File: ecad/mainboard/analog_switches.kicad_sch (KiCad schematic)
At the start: 66 parts, among them U1 CD4051BM96, U10 DRV5056A3xQDBZxR, U11 DRV5056A3xQDBZxR, U12 DRV5056A3xQDBZxR, U13 DRV5056A3xQDBZxR, U14 DRV5056A3xQDBZxR, U15 DRV5056A3xQDBZxR, U16 DRV5056A3xQDBZxR, U17 DRV5056A3xQDBZxR, U18 DRV5056A3xQDBZxR, U19 DRV5056A3xQDBZxR, U20 DRV5056A3xQDBZxR, U23 DRV5056A3xQDBZxR, U5 DRV5056A3xQDBZxR, U6 DRV5056A3xQDBZxR, U7 DRV5056A3xQDBZxR, U8 DRV5056A3xQDBZxR, U9 CD4051BM96

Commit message: place parts except analog switches
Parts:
- U22: renamed from U1; JLCPCB (none) -> C21379
- U23: renamed from U9; JLCPCB (none) -> C21379
- U6: renamed from U23; JLCPCB (none) -> C2866615
- renumbered C19 to C21, C20 to C22, C22 to C23, C25 to C24, C23 to C25, C21 to C26, C24 to C27, C26 to C28, C27 to C29, C29 to C30, C33 to C32, C28 to C33, C30 to C34, C32 to C35, C34 to C36, C35 to C37, C39 to C38, C43 to C39, C47 to C40, C37 to C41, C41 to C42, C45 to C43, C49 to C44, C36 to C45, C40 to C46, C44 to C47, C38 to C49, C42 to C50, C46 to C51, C50 to C52, R11 to R14, R12 to R15, R13 to R16, R14 to R17, R15 to R18, R16 to R19, R17 to R20, R18 to R21, R19 to R22, R21 to R23, R23 to R24, R20 to R26, R22 to R27, R24 to R28, R28 to R29, U8 to U10, U10 to U11, U11 to U12, U12 to U13, U13 to U14, U17 to U16, U19 to U17, U14 to U18, U16 to U19, U18 to U20, U20 to U21, U5 to U7, U6 to U8, U7 to U9
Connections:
- net ADC0 renamed MUX0_OUT
- net ADC1 renamed MUX1_OUT
- net GPIO10 renamed MUX0_A
- net GPIO11 renamed MUX0_B
- net GPIO12 renamed MUX0_C
- net GPIO13 renamed MUX1_A
- net GPIO14 renamed MUX1_B
- net GPIO15 renamed MUX1_C

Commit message: .
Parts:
- U10, U11, U12, U13, U14, U15, U16, U17, U18, U19, U20, U21, U6, U7, U8, U9: footprint Package_TO_SOT_SMD:SOT-23 -> Udong:SW_Cherry_MX_PCB_1.00u_hall_effect
- renumbered C25 to C22, C22 to C23, C26 to C24, C23 to C25, C27 to C26, C24 to C27, C33 to C30, C30 to C31, C34 to C32, C31 to C33, C35 to C34, C32 to C35, C41 to C38, C38 to C39, C42 to C40, C39 to C41, C43 to C42, C40 to C43, C49 to C46, C46 to C47, C50 to C48, C47 to C49, C51 to C50, C48 to C51
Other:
- moved on the sheet: C22, C24, C26, C28, C30, C32, C34, C36, C38, C40, C42, C44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

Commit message: WIP: PCB case
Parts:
- U22, U23: JCSC (none) -> C21379; JLCPCB C21379 -> (none)
- U6: JCSC (none) -> C2866615; JLCPCB C2866615 -> (none)
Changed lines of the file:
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@@
 			)
 		)
-		(property "JLCPCB" "C2866615"
+		(property "JCSC" "C2866615"
 			(at 43.18 27.94 0)
 			(effects
@@
 			)
 		)
-		(property "JLCPCB" "C21379"
+		(property "JCSC" "C21379"
 			(at 118.11 168.91 0)
 			(effects
@@
 			)
 		)
-		(property "JLCPCB" "C21379"
+		(property "JCSC" "C21379"
 			(at 48.26 168.91 0)
 			(effects

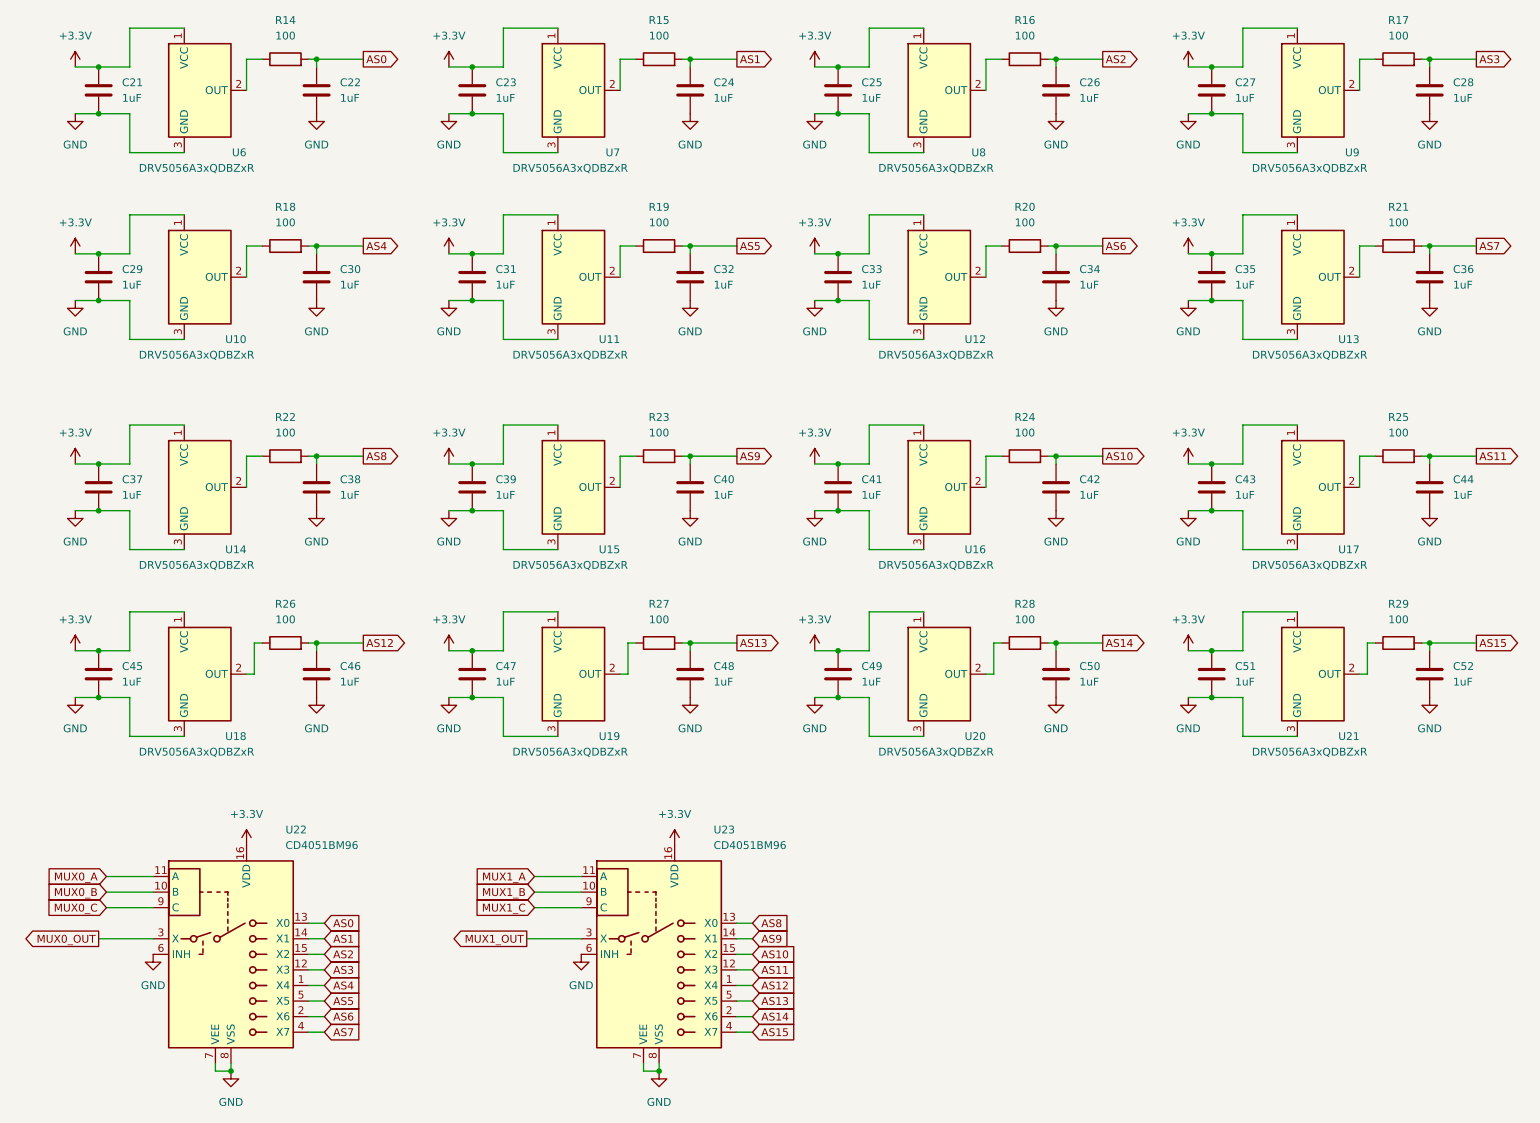
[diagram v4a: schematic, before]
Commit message: Make a DigitalSwitch field so that scripts can configure digital-switch related parts easily
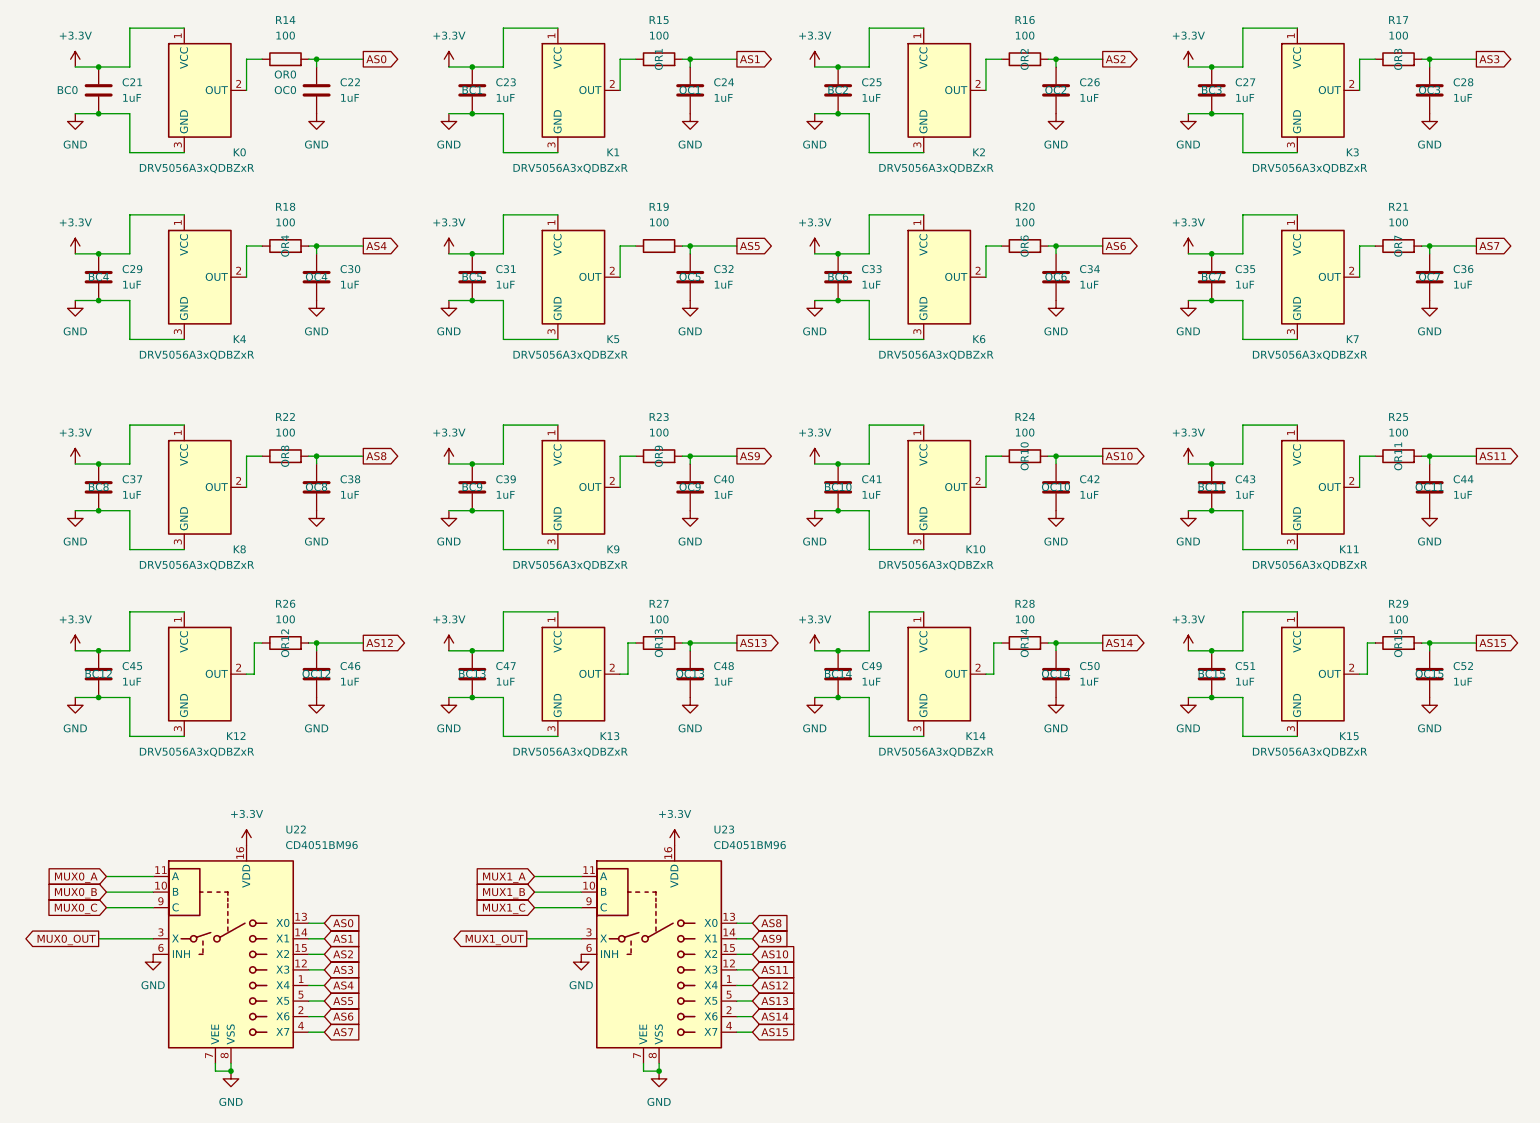
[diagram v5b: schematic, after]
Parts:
- C21: DigitalSwitch (none) -> BC0
- C22: DigitalSwitch (none) -> OC0
- C23: DigitalSwitch (none) -> BC1
- C24: DigitalSwitch (none) -> OC1
- C25: DigitalSwitch (none) -> BC2
- C26: DigitalSwitch (none) -> OC2
- C27: DigitalSwitch (none) -> BC3
- C28: DigitalSwitch (none) -> OC3
- C29: DigitalSwitch (none) -> BC4
- C30: DigitalSwitch (none) -> OC4
- C31: DigitalSwitch (none) -> BC5
- C32: DigitalSwitch (none) -> OC5
- C33: DigitalSwitch (none) -> BC6
- C34: DigitalSwitch (none) -> OC6
- C35: DigitalSwitch (none) -> BC7
- C36: DigitalSwitch (none) -> OC7
- C37: DigitalSwitch (none) -> BC8
- C38: DigitalSwitch (none) -> OC8
- C39: DigitalSwitch (none) -> BC9
- C40: DigitalSwitch (none) -> OC9
- C41: DigitalSwitch (none) -> BC10
- C42: DigitalSwitch (none) -> OC10
- C43: DigitalSwitch (none) -> BC11
- C44: DigitalSwitch (none) -> OC11
- C45: DigitalSwitch (none) -> BC12
- C46: DigitalSwitch (none) -> OC12
- C47: DigitalSwitch (none) -> BC13
- C48: DigitalSwitch (none) -> OC13
- C49: DigitalSwitch (none) -> BC14
- C50: DigitalSwitch (none) -> OC14
- C51: DigitalSwitch (none) -> BC15
- C52: DigitalSwitch (none) -> OC15
- K0: renamed from U6; footprint Udong:SW_Cherry_MX_PCB_1.00u_hall_effect -> Udong:SK20_hall_IC
- K1: renamed from U7; footprint Udong:SW_Cherry_MX_PCB_1.00u_hall_effect -> Udong:SK20_hall_IC
- K10: renamed from U16; footprint Udong:SW_Cherry_MX_PCB_1.00u_hall_effect -> Udong:SK20_hall_IC
- K11: renamed from U17; footprint Udong:SW_Cherry_MX_PCB_1.00u_hall_effect -> Udong:SK20_hall_IC
- K12: renamed from U18; footprint Udong:SW_Cherry_MX_PCB_1.00u_hall_effect -> Udong:SK20_hall_IC
- K13: renamed from U19; footprint Udong:SW_Cherry_MX_PCB_1.00u_hall_effect -> Udong:SK20_hall_IC
- K14: renamed from U20; footprint Udong:SW_Cherry_MX_PCB_1.00u_hall_effect -> Udong:SK20_hall_IC
- K15: renamed from U21; footprint Udong:SW_Cherry_MX_PCB_1.00u_hall_effect -> Udong:SK20_hall_IC
- K2: renamed from U8; footprint Udong:SW_Cherry_MX_PCB_1.00u_hall_effect -> Udong:SK20_hall_IC
- K3: renamed from U9; footprint Udong:SW_Cherry_MX_PCB_1.00u_hall_effect -> Udong:SK20_hall_IC
- K4: renamed from U10; footprint Udong:SW_Cherry_MX_PCB_1.00u_hall_effect -> Udong:SK20_hall_IC
- K5: renamed from U11; footprint Udong:SW_Cherry_MX_PCB_1.00u_hall_effect -> Udong:SK20_hall_IC
- K6: renamed from U12; footprint Udong:SW_Cherry_MX_PCB_1.00u_hall_effect -> Udong:SK20_hall_IC
- K7: renamed from U13; footprint Udong:SW_Cherry_MX_PCB_1.00u_hall_effect -> Udong:SK20_hall_IC
- K8: renamed from U14; footprint Udong:SW_Cherry_MX_PCB_1.00u_hall_effect -> Udong:SK20_hall_IC
- K9: renamed from U15; footprint Udong:SW_Cherry_MX_PCB_1.00u_hall_effect -> Udong:SK20_hall_IC
- R14: DigitalSwitch (none) -> OR0
- R15: DigitalSwitch (none) -> OR1
- R16: DigitalSwitch (none) -> OR2
- R17: DigitalSwitch (none) -> OR3
- R18: DigitalSwitch (none) -> OR4
- R19: DigitalSwitch (none) -> OR5
- R20: DigitalSwitch (none) -> OR6
- R21: DigitalSwitch (none) -> OR7
- R22: DigitalSwitch (none) -> OR8
- R23: DigitalSwitch (none) -> OR9
- R24: DigitalSwitch (none) -> OR10
- R25: DigitalSwitch (none) -> OR11
- R26: DigitalSwitch (none) -> OR12
- R27: DigitalSwitch (none) -> OR13
- R28: DigitalSwitch (none) -> OR14
- R29: DigitalSwitch (none) -> OR15

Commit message: Python script to update switch positions
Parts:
- K0: DigitalSwitch (none) -> K0
- K1: DigitalSwitch (none) -> K1
- K10: DigitalSwitch (none) -> K10
- K11: DigitalSwitch (none) -> K11
- K12: DigitalSwitch (none) -> K12
- K13: DigitalSwitch (none) -> K13
- K14: DigitalSwitch (none) -> K14
- K15: DigitalSwitch (none) -> K15
- K2: DigitalSwitch (none) -> K2
- K3: DigitalSwitch (none) -> K3
- K4: DigitalSwitch (none) -> K4
- K5: DigitalSwitch (none) -> K5
- K6: DigitalSwitch (none) -> K6
- K7: DigitalSwitch (none) -> K7
- K8: DigitalSwitch (none) -> K8
- K9: DigitalSwitch (none) -> K9
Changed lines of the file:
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@@
 			)
 		)
-		(property "フィールド5" ""
+		(property "DigitalSwitch" "K5"
 			(at 104.14 58.42 0)
 			(effects
@@
 			)
 		)
-		(property "フィールド5" ""
+		(property "DigitalSwitch" "K15"
 			(at 224.79 123.19 0)
 			(effects
@@
 			)
 		)
-		(property "フィールド5" ""
+		(property "DigitalSwitch" "K2"
 			(at 163.83 27.94 0)
 			(effects
@@
 			)
 		)
-		(property "フィールド5" ""
+		(property "DigitalSwitch" "K10"
 			(at 163.83 92.71 0)
 			(effects
@@
 			)
 		)
-		(property "フィールド5" ""
+		(property "DigitalSwitch" "K12"
 			(at 43.18 123.19 0)
 			(effects
@@
 			)
 		)
-		(property "フィールド5" ""
+		(property "DigitalSwitch" "K3"
 			(at 224.79 27.94 0)
 			(effects
@@
 			)
 		)
-		(property "フィールド5" ""
+		(property "DigitalSwitch" "K0"
 			(at 43.18 27.94 0)
 			(effects
@@
 			)
 		)
-		(property "フィールド5" ""
+		(property "DigitalSwitch" "K6"
 			(at 163.83 58.42 0)
 			(effects
@@
 			)
 		)
-		(property "フィールド5" ""
-			(at 104.14 27.94 0)
-			(effects
-				(font
-					(size 1.27 1.27)
-				)
-				(hide yes)
-			)
-		)
-		(property "フィールド6" ""
+		(property "DigitalSwitch" "K1"
 			(at 104.14 27.94 0)
 			(effects
@@
 			)
 		)
-		(property "フィールド5" ""
+		(property "DigitalSwitch" "K11"
 			(at 224.79 92.71 0)
 			(effects
@@
 			)
 		)
-		(property "フィールド5" ""
+		(property "DigitalSwitch" "K8"
 			(at 43.18 92.71 0)
 			(effects
@@
 			)
 		)
-		(property "フィールド5" ""
+		(property "DigitalSwitch" "K7"
 			(at 224.79 58.42 0)
 			(effects
@@
 			)
 		)
-		(property "フィールド5" ""
+		(property "DigitalSwitch" "K9"
 			(at 104.14 92.71 0)
 			(effects
@@
 			)
 		)
-		(property "フィールド5" ""
+		(property "DigitalSwitch" "K13"
 			(at 104.14 123.19 0)
 			(effects
@@
 			)
 		)
-		(property "フィールド5" ""
+		(property "DigitalSwitch" "K4"
 			(at 43.18 58.42 0)
 			(effects
@@
 			)
 		)
-		(property "フィールド5" ""
+		(property "DigitalSwitch" "K14"
 			(at 163.83 123.19 0)
 			(effects

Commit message: rev2 board
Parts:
- K0: JCSC C2866615 -> (none); LCSC (none) -> C2866615
- K1, K10, K11, K12, K13, K14, K15, K2, K3, K4, K5, K6, K7, K8, K9: LCSC (none) -> C2866615
- U22, U23: JCSC C21379 -> (none); LCSC (none) -> C21379
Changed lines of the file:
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@@
 			)
 		)
-		(property "フィールド6" ""
+		(property "LCSC" "C2866615"
 			(at 104.14 58.42 0)
 			(effects
@@
 			)
 		)
-		(property "フィールド6" ""
+		(property "LCSC" "C2866615"
 			(at 224.79 123.19 0)
 			(effects
@@
 			)
 		)
-		(property "フィールド6" ""
+		(property "LCSC" "C2866615"
 			(at 163.83 27.94 0)
 			(effects
@@
 			)
 		)
-		(property "フィールド6" ""
+		(property "LCSC" "C2866615"
 			(at 163.83 92.71 0)
 			(effects
@@
 			)
 		)
-		(property "フィールド6" ""
+		(property "LCSC" "C2866615"
 			(at 43.18 123.19 0)
 			(effects
@@
 			)
 		)
-		(property "フィールド6" ""
+		(property "LCSC" "C2866615"
 			(at 224.79 27.94 0)
 			(effects
@@
 			)
 		)
-		(property "JCSC" "C2866615"
+		(property "DigitalSwitch" "K0"
 			(at 43.18 27.94 0)
 			(effects
@@
 			)
 		)
-		(property "DigitalSwitch" "K0"
+		(property "LCSC" "C2866615"
 			(at 43.18 27.94 0)
 			(effects
@@
 			)
 		)
-		(property "フィールド6" ""
+		(property "LCSC" "C2866615"
 			(at 163.83 58.42 0)
 			(effects
@@
 			)
 		)
+		(property "LCSC" "C2866615"
+			(at 104.14 27.94 0)
+			(effects
+				(font
+					(size 1.27 1.27)
+				)
+				(hide yes)
+			)
+		)
 		(pin "3"
 		)
@@
 			)
 		)
-		(property "フィールド6" ""
+		(property "LCSC" "C2866615"
 			(at 224.79 92.71 0)
 			(effects
@@
 			)
 		)
-		(property "JCSC" "C21379"
+		(property "LCSC" "C21379"
 			(at 118.11 168.91 0)
 			(effects
@@
 			)
 		)
-		(property "フィールド6" ""
+		(property "LCSC" "C2866615"
 			(at 43.18 92.71 0)
 			(effects
@@
 			)
 		)
-		(property "フィールド6" ""
+		(property "LCSC" "C2866615"
 			(at 224.79 58.42 0)
 			(effects
@@
 			)
 		)
-		(property "フィールド6" ""
+		(property "LCSC" "C2866615"
 			(at 104.14 92.71 0)
 			(effects
@@
 			)
 		)
-		(property "フィールド6" ""
+		(property "LCSC" "C2866615"
 			(at 104.14 123.19 0)
 			(effects
@@
 			)
 		)
-		(property "フィールド6" ""
+		(property "LCSC" "C2866615"
 			(at 43.18 58.42 0)
 			(effects
@@
 			)
 		)
-		(property "フィールド6" ""
+		(property "LCSC" "C2866615"
 			(at 163.83 123.19 0)
 			(effects
@@
 			)
 		)
-		(property "JCSC" "C21379"
+		(property "LCSC" "C21379"
 			(at 48.26 168.91 0)
 			(effects
